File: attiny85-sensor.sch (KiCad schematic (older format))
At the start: 11 parts, among them IC1 ATTINY85-P, P1 PIR, P2 BIND_BTN, P3 CONN_01X02, P4 CONN_01X06

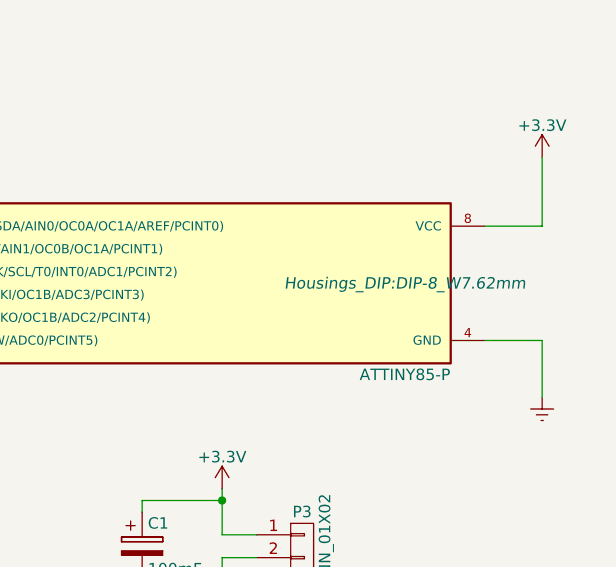
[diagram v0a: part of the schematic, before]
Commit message: Socket for the chip
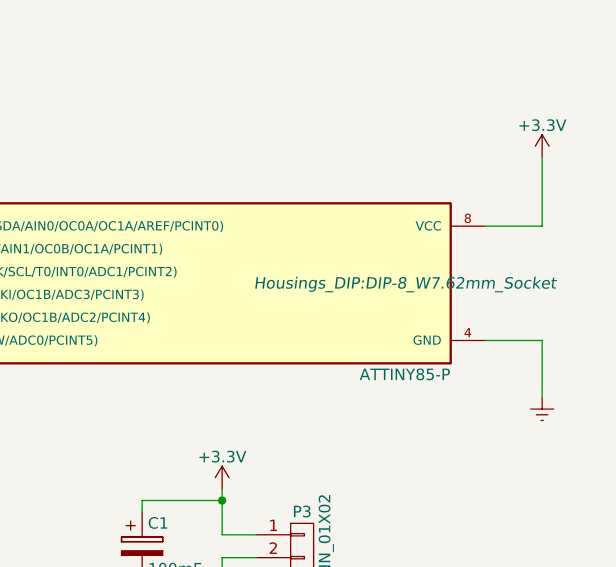
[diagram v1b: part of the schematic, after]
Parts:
- IC1: footprint Housings_DIP:DIP-8_W7.62mm -> Housings_DIP:DIP-8_W7.62mm_Socket
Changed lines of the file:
@@
 F 0 "IC1" H 5950 3350 50  0000 C CNN
 F 1 "ATTINY85-P" H 8100 2550 50  0000 C CNN
-F 2 "Housings_DIP:DIP-8_W7.62mm" H 8100 2950 50  0000 C CIN
+F 2 "Housings_DIP:DIP-8_W7.62mm_Socket" H 8100 2950 50  0000 C CIN
 F 3 "" H 7100 2950 50  0000 C CNN
 	1    7100 2950
